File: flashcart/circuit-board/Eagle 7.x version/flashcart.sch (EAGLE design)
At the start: 17 parts, among them U1 MCP1700T-3302E/TT, U2 TXB0104D, U3 W25Q128FV

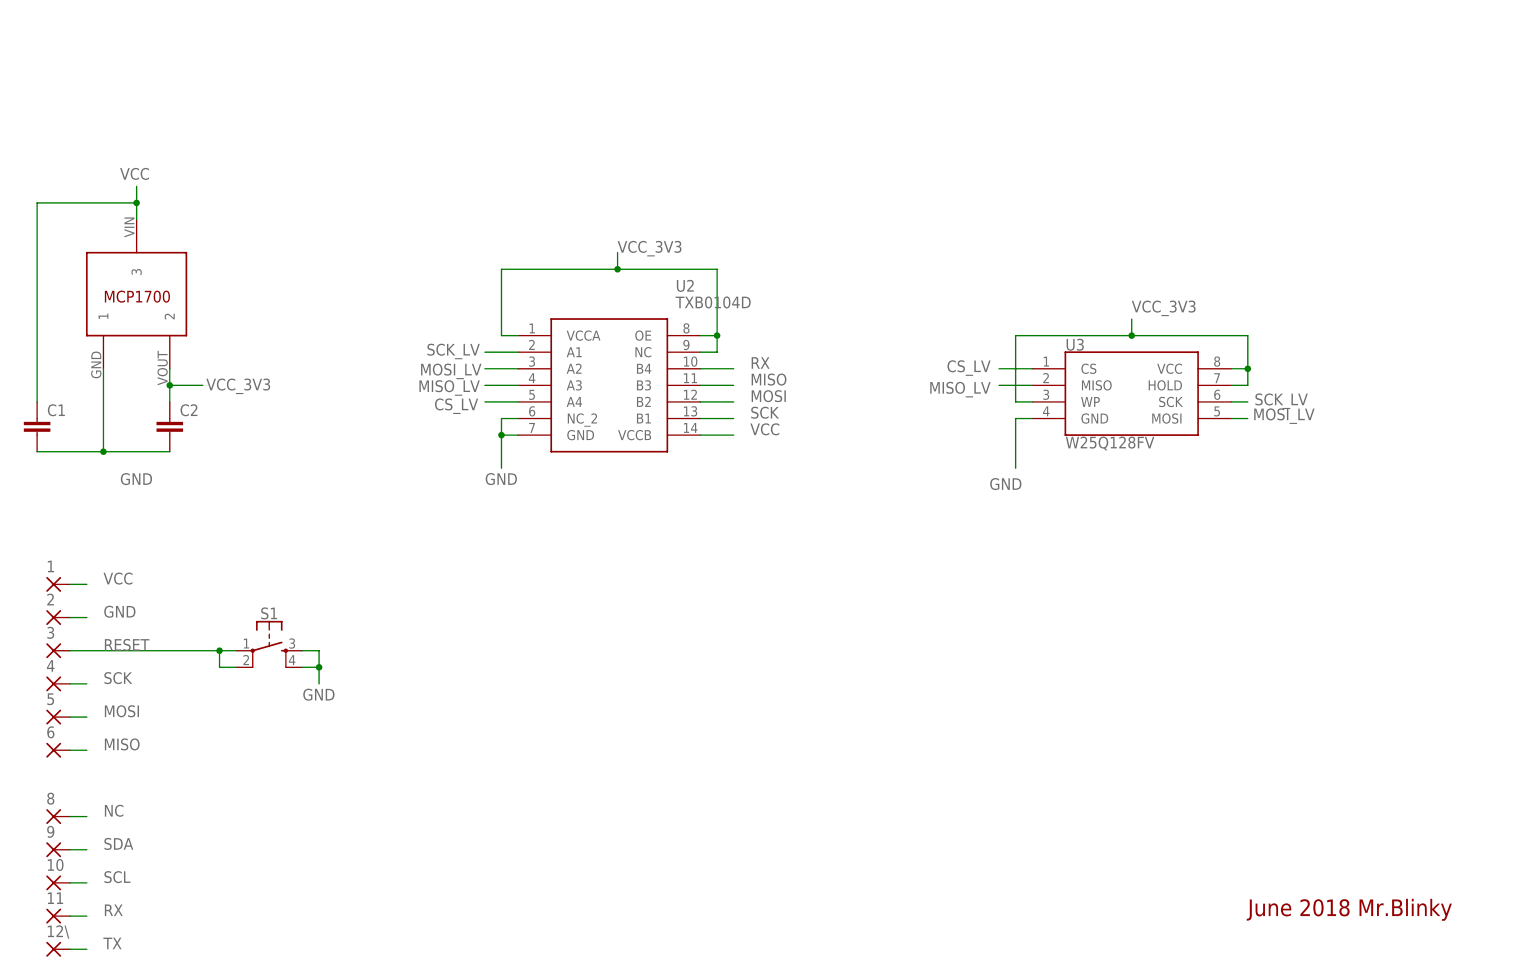
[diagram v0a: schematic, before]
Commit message: rev1.1 + gerbers
Changed connector pads, minor tweaks, added Blinky icon, added gerbers
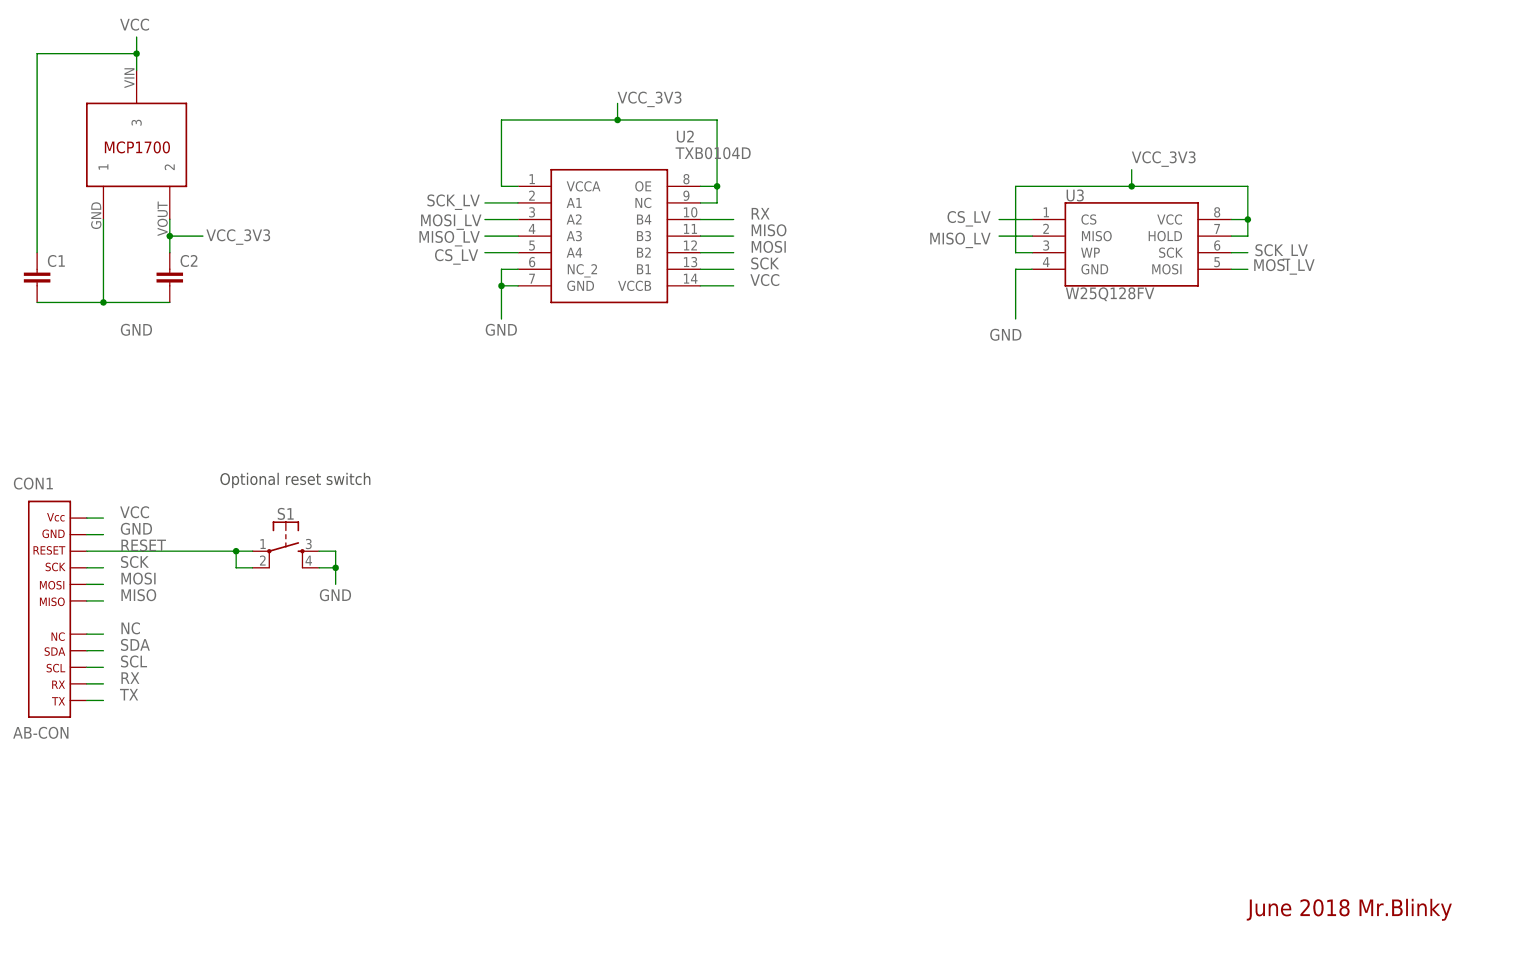
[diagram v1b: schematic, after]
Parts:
- removed 1, 10, 11, 12\, 2, 3, 4, 5, 6, 8, 9: (no value), wirepad:SMD2
- added CON1: AB-CON, ab-expansion-con:AB-CON
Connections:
- net GND: now also CON1.P2; no longer 2.P
- net MISO: now also CON1.P6; no longer 6.P
- net MOSI: now also CON1.P5; no longer 5.P
- net NC: now also CON1.P8; no longer 8.P
- net RESET: now also CON1.P3; no longer 3.P
- net RX: now also CON1.P11; no longer 11.P
- net SCK: now also CON1.P4; no longer 4.P
- net SCL: now also CON1.P10; no longer 10.P
- net SDA: now also CON1.P9; no longer 9.P
- net TX: now also CON1.P12; no longer 12\.P
- net VCC: now also CON1.P1; no longer 1.P
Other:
- note added: "Optional reset switch"
- moved on the sheet: C1, C2, S1, U2, U3
